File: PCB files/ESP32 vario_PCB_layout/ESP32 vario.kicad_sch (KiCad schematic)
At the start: 9 parts, among them U1 HT-RA62, U2 ESP32-S3 Waveshare, U3 BMP580, U4 LC76G GPS

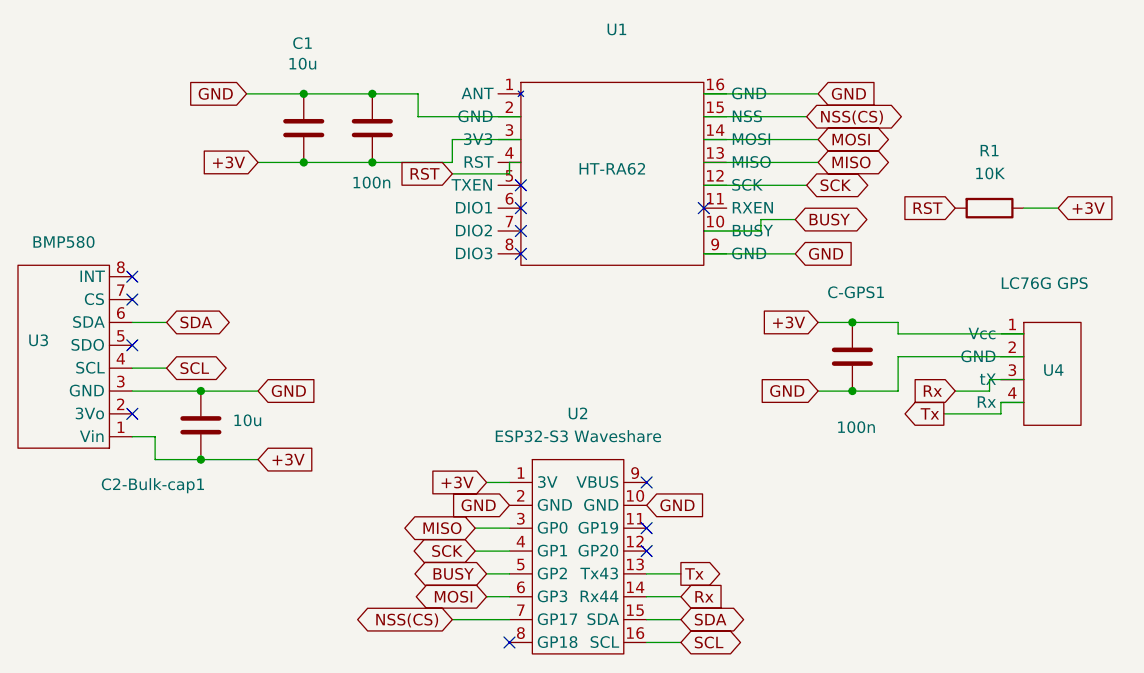
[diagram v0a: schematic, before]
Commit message: New PCB Layout
Fully rebuilt PCB from scratch, LoRa module is now compatible with FANET, Key button to be moved to BOOT key. More work to do.
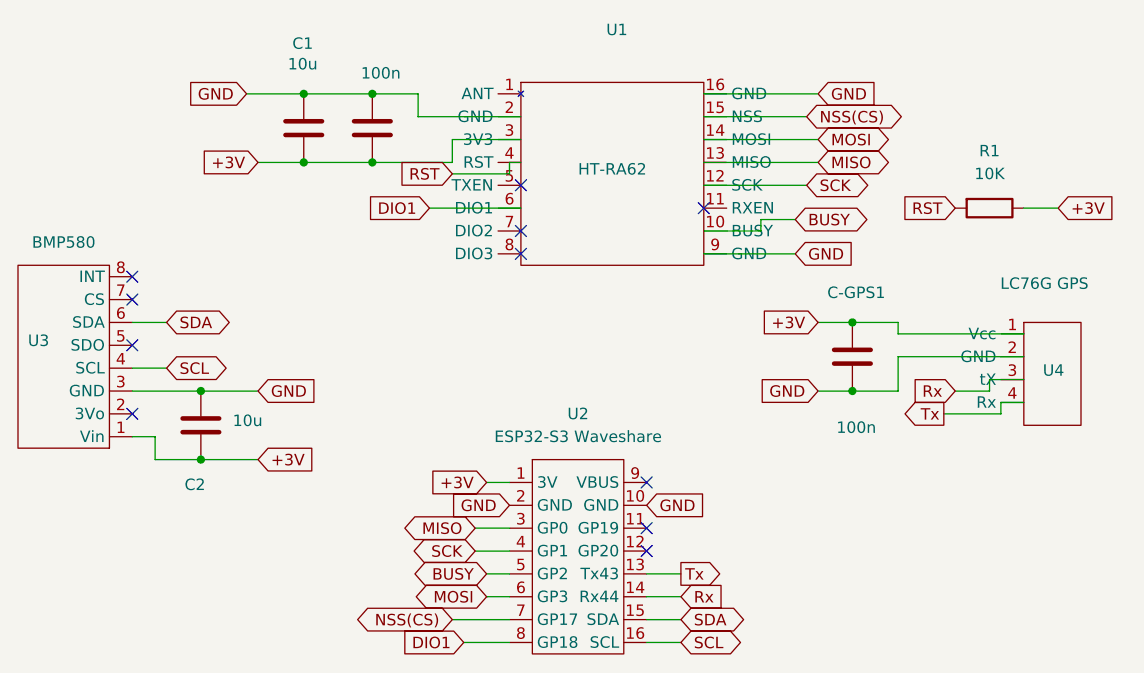
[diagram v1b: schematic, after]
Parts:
- U1: footprint Flight cumputer footprints:HT-RA62 -> NiceNano-Everything:HT-RA62
- U3: footprint Flight cumputer footprints:BMP580 Header -> Connector_PinHeader_2.54mm:PinHeader_1x08_P2.54mm_Vertical
- renumbered C2-Bulk-cap1 to C2
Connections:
- net DIO1: now reaches U2.8 (GP18)
- net DIO1: now also U1.6 (DIO1)
- no-connect marks 13 -> 11
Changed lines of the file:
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@@
-	)
-	(no_connect
-		(at 127 115.57)
 	)
 	(no_connect
@@
 	)
 	(no_connect
-		(at 128.27 67.31)
-	)
-	(no_connect
 		(at 128.27 69.85)
 	)
@@
 	(wire
 		(pts
+			(xy 121.92 115.57) (xy 127 115.57)
+		)
+		(stroke
+			(width 0)
+			(type default)
+		)
+	)
+	(wire
+		(pts
 			(xy 180.34 87.63) (xy 176.53 87.63)
 		)
@@
 		(pts
 			(xy 124.46 97.79) (xy 127 97.79)
+		)
+		(stroke
+			(width 0)
+			(type default)
+		)
+	)
+	(wire
+		(pts
+			(xy 118.11 67.31) (xy 128.27 67.31)
 		)
 		(stroke
@@
 		)
 	)
+	(global_label "DIO1"
+		(shape input)
+		(at 118.11 67.31 180)
+		(fields_autoplaced yes)
+		(effects
+			(font
+				(size 1.27 1.27)
+			)
+			(justify right)
+		)
+		(property "Intersheetrefs" "${INTERSHEET_REFS}"
+			(at 110.71 67.31 0)
+			(hide yes)
+			(show_name no)
+			(do_not_autoplace no)
+			(effects
+				(font
+					(size 1.27 1.27)
+				)
+				(justify right)
+			)
+		)
+	)
 	(global_label "MISO"
 		(shape bidirectional)
@@
 		(property "Intersheetrefs" "${INTERSHEET_REFS}"
 			(at 92.2043 62.23 0)
+			(hide yes)
+			(show_name no)
+			(do_not_autoplace no)
+			(effects
+				(font
+					(size 1.27 1.27)
+				)
+				(justify right)
+			)
+		)
+	)
+	(global_label "DIO1"
+		(shape input)
+		(at 121.92 115.57 180)
+		(fields_autoplaced yes)
+		(effects
+			(font
+				(size 1.27 1.27)
+			)
+			(justify right)
+		)
+		(property "Intersheetrefs" "${INTERSHEET_REFS}"
+			(at 114.52 115.57 0)
 			(hide yes)
 			(show_name no)
@@
 		(in_pos_files yes)
 		(dnp no)
-		(property "Reference" "C2-Bulk-cap1"
+		(property "Reference" "C2"
 			(at 93.218 98.044 0)
 			(show_name no)
@@
 			(project "ESP32 vario"
 				(path "/90e9b6f9-5e99-4c00-9d91-847e39c057df"
-					(reference "C2-Bulk-cap1")
+					(reference "C2")
 					(unit 1)
 				)
@@
 		)
 		(property "Value" "100n"
-			(at 109.474 64.516 0)
+			(at 110.49 52.324 0)
 			(show_name no)
 			(do_not_autoplace no)
@@
 			)
 		)
-		(property "Footprint" "Flight cumputer footprints:BMP580 Header"
+		(property "Footprint" "Connector_PinHeader_2.54mm:PinHeader_1x08_P2.54mm_Vertical"
 			(at 78.232 100.838 0)
 			(hide yes)
@@
 			)
 		)
-		(property "Footprint" "Flight cumputer footprints:HT-RA62"
+		(property "Footprint" "NiceNano-Everything:HT-RA62"
 			(at 135.128 45.974 0)
 			(hide yes)

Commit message: Removed DIO18 as it conflicts with Key pin
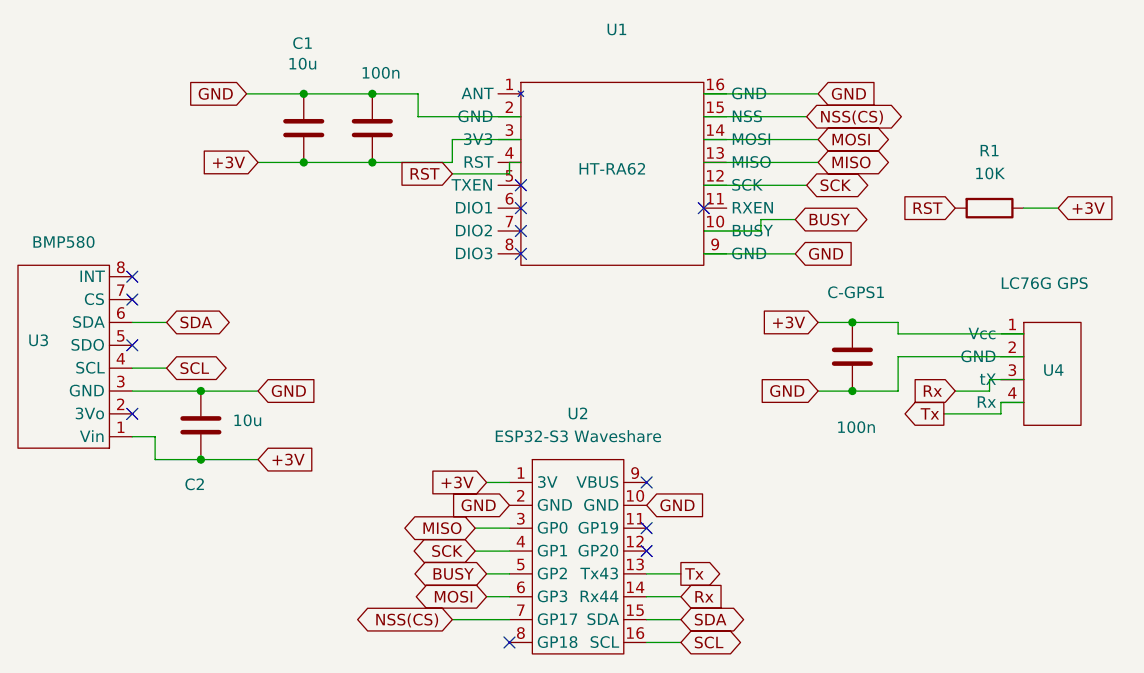
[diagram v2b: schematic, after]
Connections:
- net DIO1: no longer names the net of U2.8 (GP18)
- net DIO1: no longer U1.6 (DIO1)
- no-connect marks 11 -> 13
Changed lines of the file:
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@@
+	)
+	(no_connect
+		(at 128.27 67.31)
+	)
+	(no_connect
+		(at 127 115.57)
 	)
 	(no_connect
@@
 	(wire
 		(pts
-			(xy 121.92 115.57) (xy 127 115.57)
-		)
-		(stroke
-			(width 0)
-			(type default)
-		)
-	)
-	(wire
-		(pts
 			(xy 180.34 87.63) (xy 176.53 87.63)
 		)
@@
 		(pts
 			(xy 124.46 97.79) (xy 127 97.79)
-		)
-		(stroke
-			(width 0)
-			(type default)
-		)
-	)
-	(wire
-		(pts
-			(xy 118.11 67.31) (xy 128.27 67.31)
 		)
 		(stroke
@@
 		)
 	)
-	(global_label "DIO1"
-		(shape input)
-		(at 118.11 67.31 180)
+	(global_label "MISO"
+		(shape bidirectional)
+		(at 123.19 102.87 180)
 		(fields_autoplaced yes)
 		(effects
@@
 		)
 		(property "Intersheetrefs" "${INTERSHEET_REFS}"
-			(at 110.71 67.31 0)
+			(at 114.4973 102.87 0)
 			(hide yes)
 			(show_name no)
@@
 		)
 	)
-	(global_label "MISO"
-		(shape bidirectional)
-		(at 123.19 102.87 180)
-		(fields_autoplaced yes)
-		(effects
-			(font
-				(size 1.27 1.27)
-			)
-			(justify right)
-		)
-		(property "Intersheetrefs" "${INTERSHEET_REFS}"
-			(at 114.4973 102.87 0)
-			(hide yes)
-			(show_name no)
-			(do_not_autoplace no)
-			(effects
-				(font
-					(size 1.27 1.27)
-				)
-				(justify right)
-			)
-		)
-	)
 	(global_label "MOSI"
 		(shape bidirectional)
@@
 			(hide yes)
 			(show_name no)
-			(do_not_autoplace no)
-			(effects
-				(font
-					(size 1.27 1.27)
-				)
-				(justify right)
-			)
-		)
-	)
-	(global_label "DIO1"
-		(shape input)
-		(at 121.92 115.57 180)
-		(fields_autoplaced yes)
-		(effects
-			(font
-				(size 1.27 1.27)
-			)
-			(justify right)
-		)
-		(property "Intersheetrefs" "${INTERSHEET_REFS}"
-			(at 114.52 115.57 0)
-			(hide yes)
-			(show_name no)
